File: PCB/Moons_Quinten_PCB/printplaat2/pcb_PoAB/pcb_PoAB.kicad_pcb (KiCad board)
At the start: 2 copper layers, 32.5 x 73.8 mm, 34 parts, among them U9 ARDUINO_MKR_WAN_1310

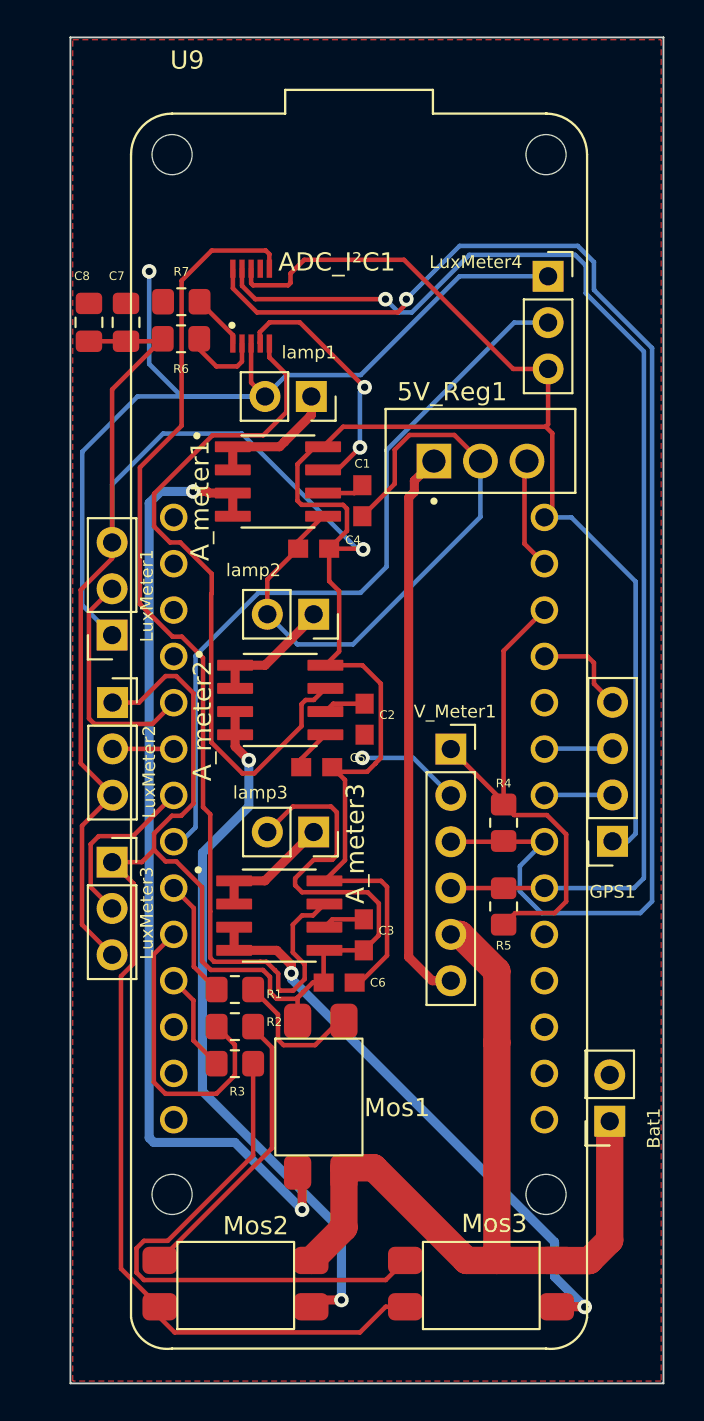
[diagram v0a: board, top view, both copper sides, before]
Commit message: printplaat en lichtmeter aangepast
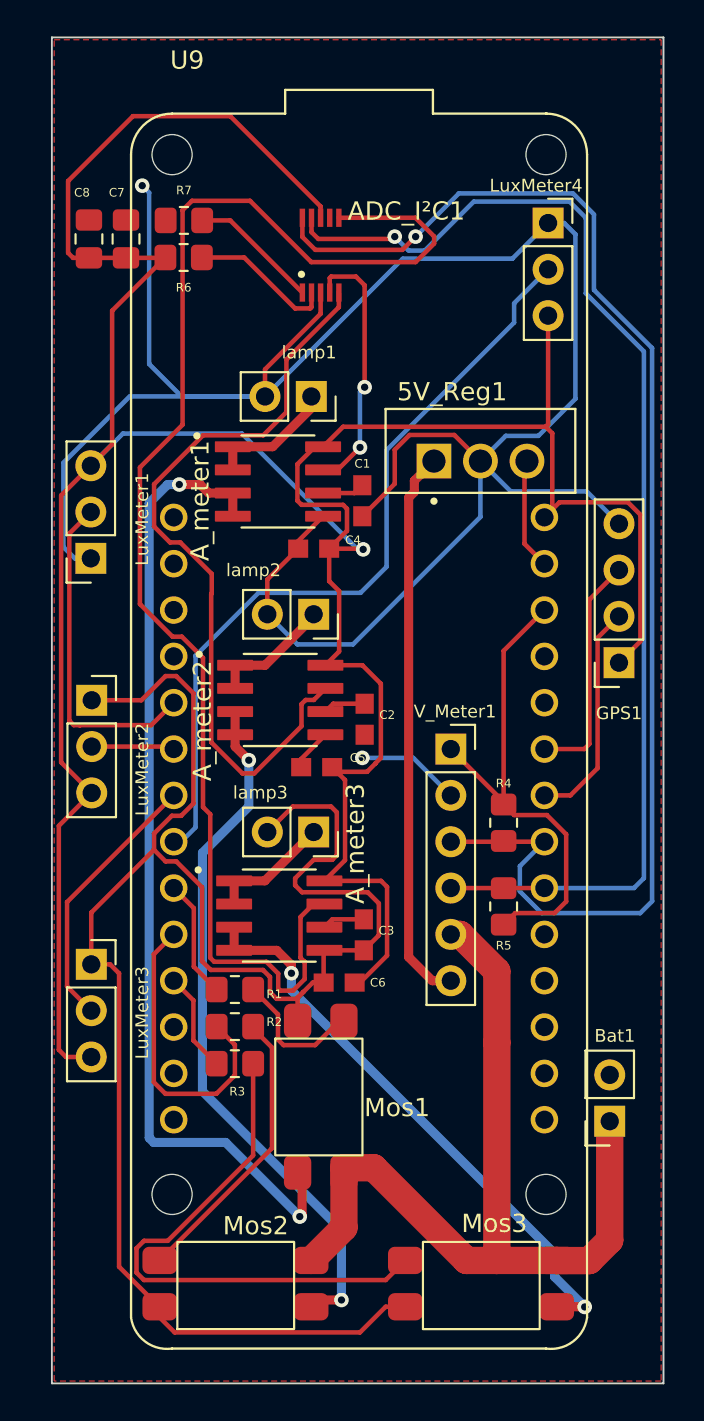
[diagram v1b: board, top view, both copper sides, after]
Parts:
- moved GPS1 9.80 mm to (105.3, 81.3)
- moved LuxMeter3 5.72 mm to (76.3, 97.8)
- moved ADC_I²C1 4.72 mm to (88.9, 58.9)
- moved C7 4.57 mm to (78.2, 58.0)
- moved C8 4.57 mm to (76.2, 58.0)
- moved R6 4.46 mm to (81.4, 59.1)
- moved R7 4.46 mm to (81.4, 57.0)
- moved LuxMeter1 4.37 mm to (76.3, 75.5)
- moved LuxMeter4 2.92 mm to (101.4, 57.2)
- moved LuxMeter2 1.15 mm to (76.4, 83.3)
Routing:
- net GND: track 203.7 -> 232.7 mm
- net /stroom3: track 58.5 -> 77.5 mm
- net /TX: track 3.79 -> 12.8 mm
- net /RX: track 3.79 -> 12.3 mm
- net /5V_bord: track 171.4 -> 178.9 mm
- net /Lichtmeting1: track 12.9 -> 18.3 mm
- net /Lichtmeting3: track 9.67 -> 14.8 mm
- net Net-(R7-Pad2): track 3.05 -> 7.13 mm
- net /stroom2: track 38.1 -> 42.0 mm
- net Net-(R6-Pad1): track 4.40 -> 8.00 mm
- net /Lichtmeting4: track 41.6 -> 43.4 mm
- net /SCL: track 76.3 -> 74.5 mm
- net /SDA: track 67.7 -> 66.2 mm
- net /Lichtmeting2: track 3.36 -> 4.55 mm
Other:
- board size 32.5 x 73.8 mm -> 33.5 x 73.8 mm

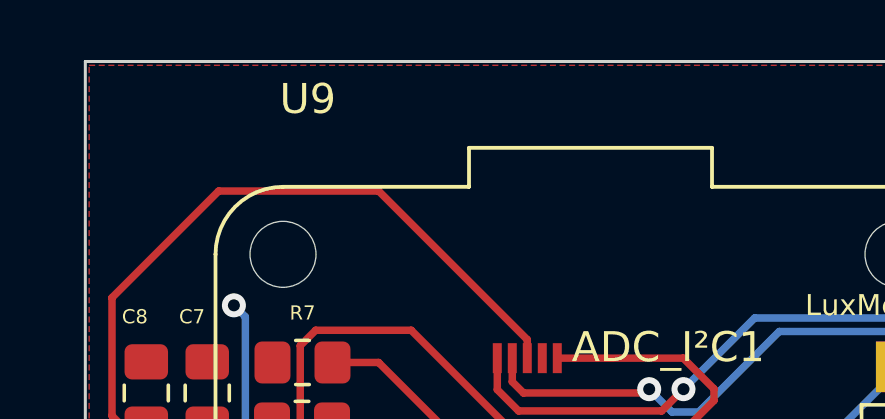
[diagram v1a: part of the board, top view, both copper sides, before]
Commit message: pcb baseplate en docs aangepast
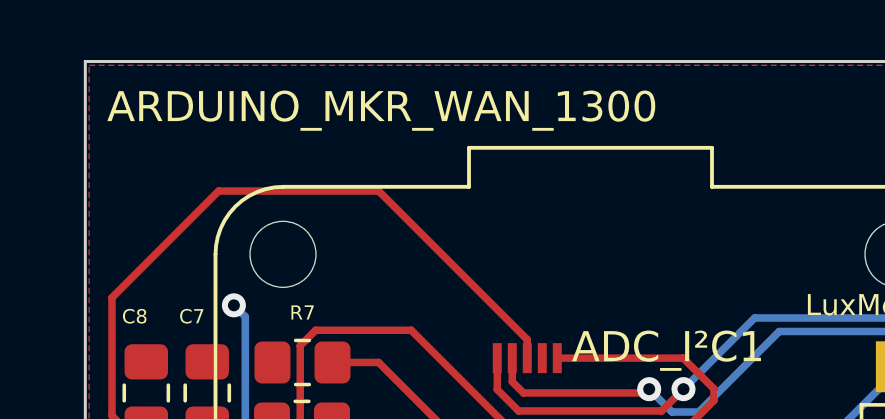
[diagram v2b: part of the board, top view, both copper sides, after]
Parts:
- renumbered U9 to ARDUINO_MKR_WAN_1300
